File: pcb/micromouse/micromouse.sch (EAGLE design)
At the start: 57 parts, among them J1 Connector_M1, J2 Connector_M1, J4 Programmer

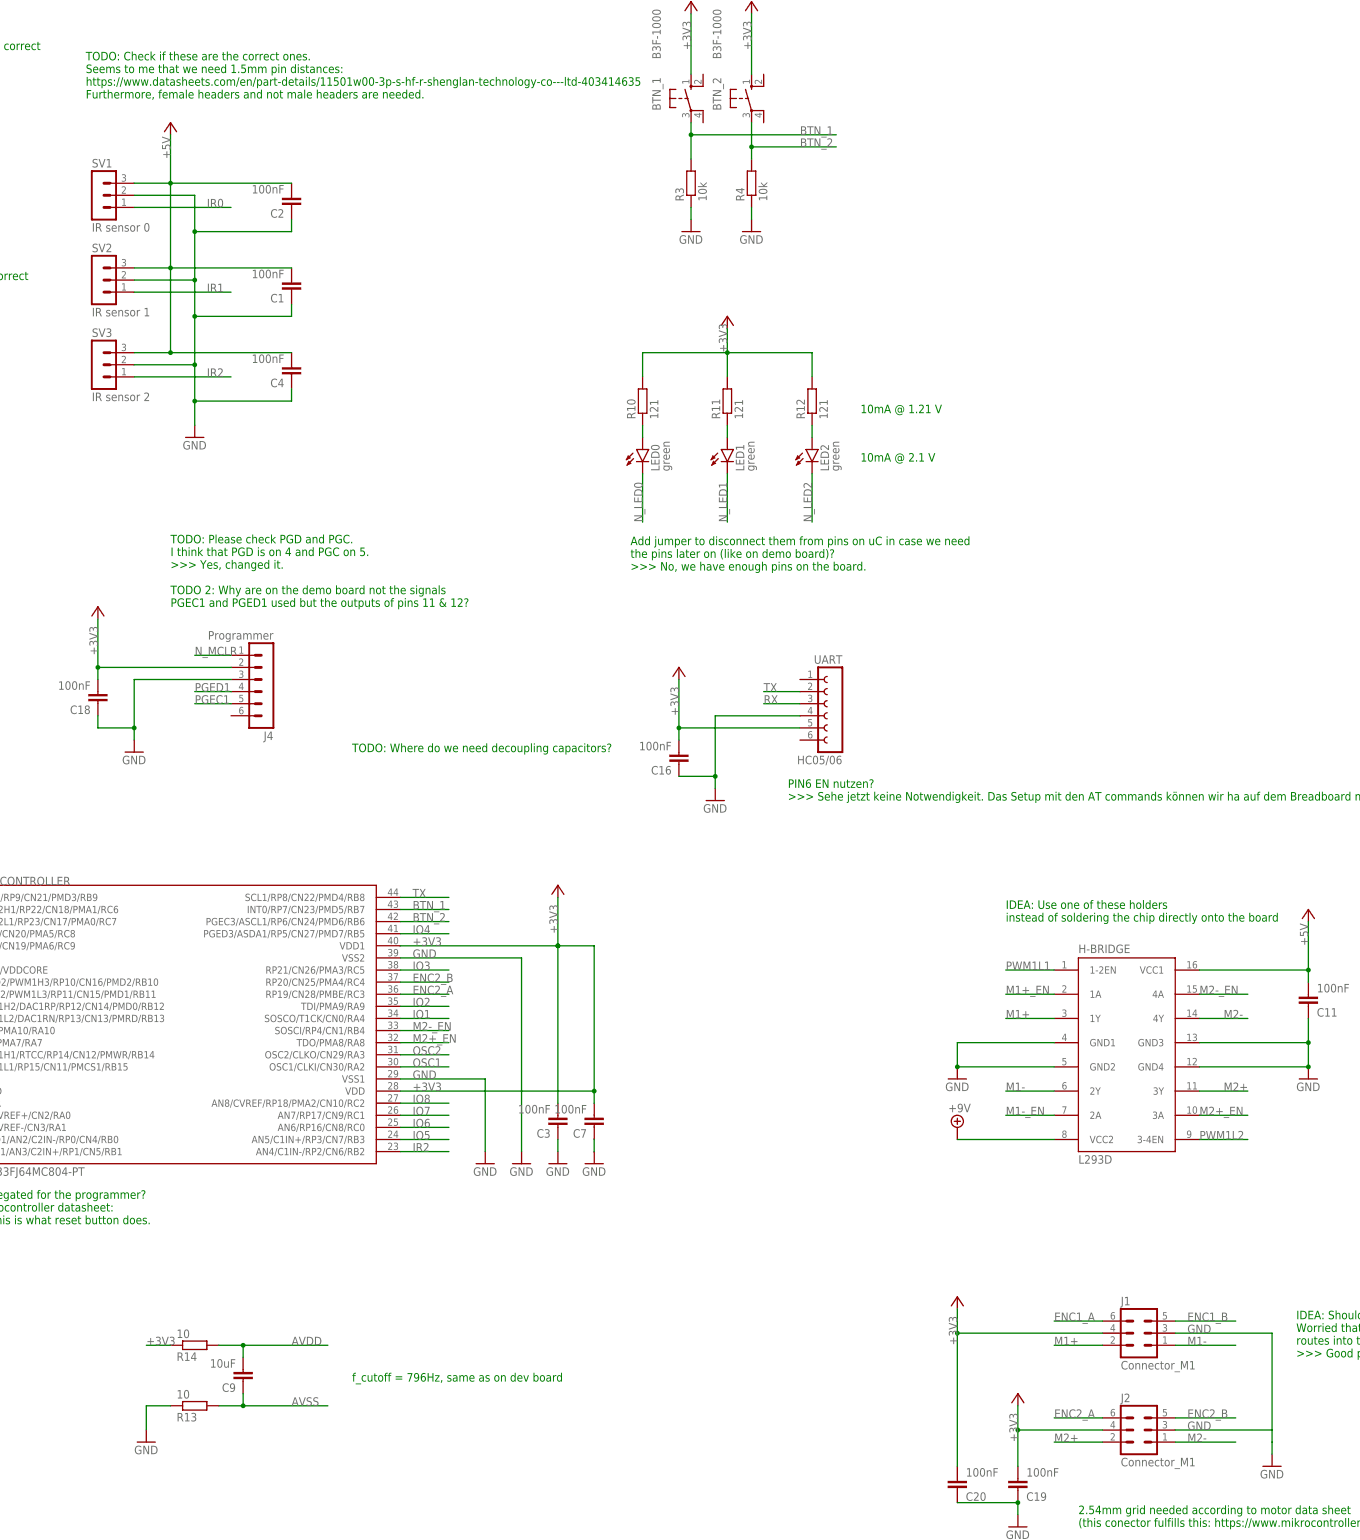
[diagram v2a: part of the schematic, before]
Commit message: Add missing junction (two wires were not correctly connected).
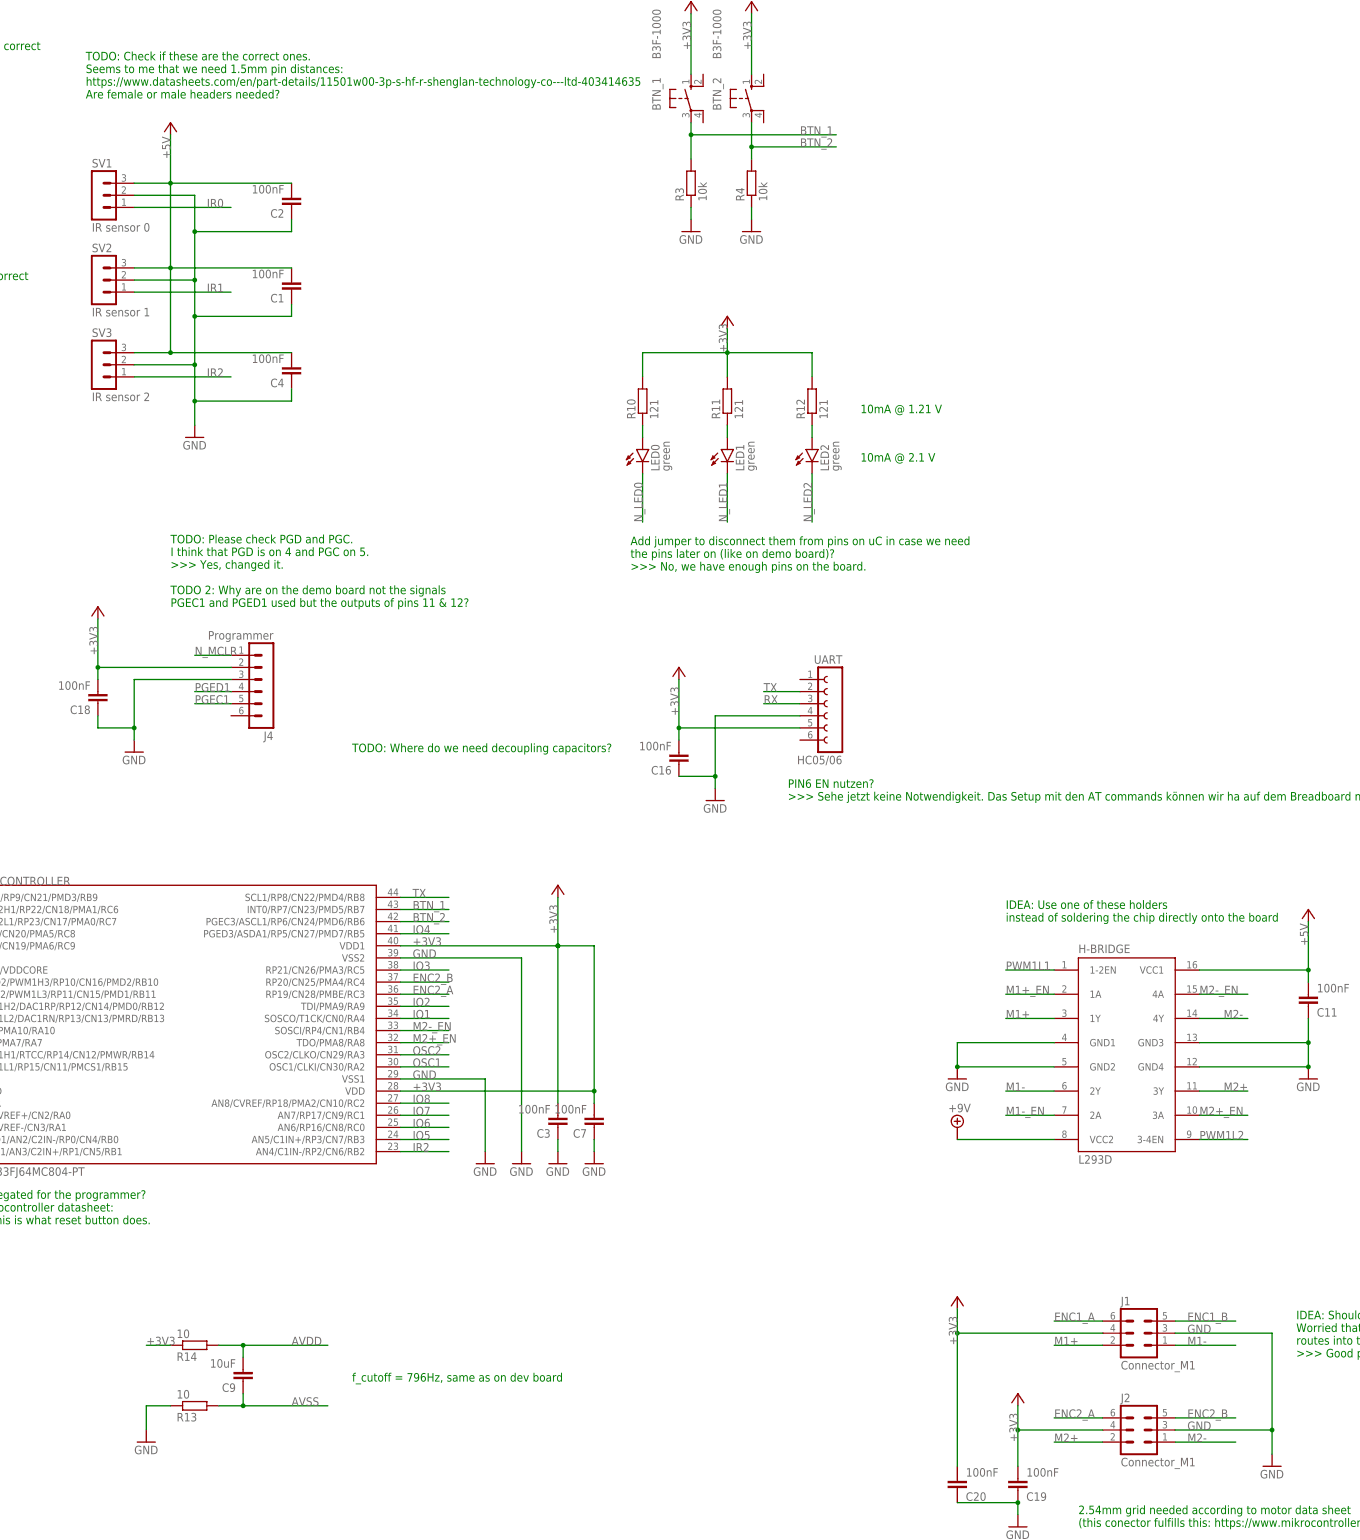
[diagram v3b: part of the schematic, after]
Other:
- note added: "TODO: Check if these are the correct ones. Seems to me that we need 1.5mm pin distances: https://www.datasheets.com/en/part-details/11501w00-3p-s-hf-r-shenglan-technology-co---ltd-403414635 Are female or male headers needed?"
- note removed: "TODO: Check if these are the correct ones. Seems to me that we need 1.5mm pin distances: https://www.datasheets.com/en/part-details/11501w00-3p-s-hf-r-shenglan-technology-co---ltd-403414635 Furthermore, female headers and not male headers are needed."
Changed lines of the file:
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@@
 Seems to me that we need 1.5mm pin distances:
 https://www.datasheets.com/en/part-details/11501w00-3p-s-hf-r-shenglan-technology-co---ltd-403414635
-Furthermore, female headers and not male headers are needed.</text>
+Are female or male headers needed?</text>
 <text x="-71.12" y="358.14" size="1.778" layer="91">Connects either 2-3 or 2-1,
 depending on switch position.</text>
@@
 </segment>
 <segment>
-<pinref part="J2" gate="1" pin="3"/>
-<wire x1="330.2" y1="48.26" x2="350.52" y2="48.26" width="0.1524" layer="91"/>
 <label x="332.74" y="48.26" size="1.778" layer="95"/>
 <pinref part="GND25" gate="1" pin="GND"/>
-<wire x1="350.52" y1="48.26" x2="350.52" y2="45.72" width="0.1524" layer="91"/>
-<wire x1="350.52" y1="45.72" x2="350.52" y2="43.18" width="0.1524" layer="91"/>
 <wire x1="330.2" y1="68.58" x2="350.52" y2="68.58" width="0.1524" layer="91"/>
 <pinref part="J1" gate="1" pin="3"/>
 <label x="332.74" y="68.58" size="1.778" layer="95"/>
 <wire x1="350.52" y1="68.58" x2="350.52" y2="48.26" width="0.1524" layer="91"/>
-</segment>
-<segment>
+<pinref part="J2" gate="1" pin="3"/>
+<wire x1="350.52" y1="48.26" x2="350.52" y2="43.18" width="0.1524" layer="91"/>
+<wire x1="330.2" y1="48.26" x2="350.52" y2="48.26" width="0.1524" layer="91"/>
+<junction x="350.52" y="48.26"/>
+</segment>
+<segment>

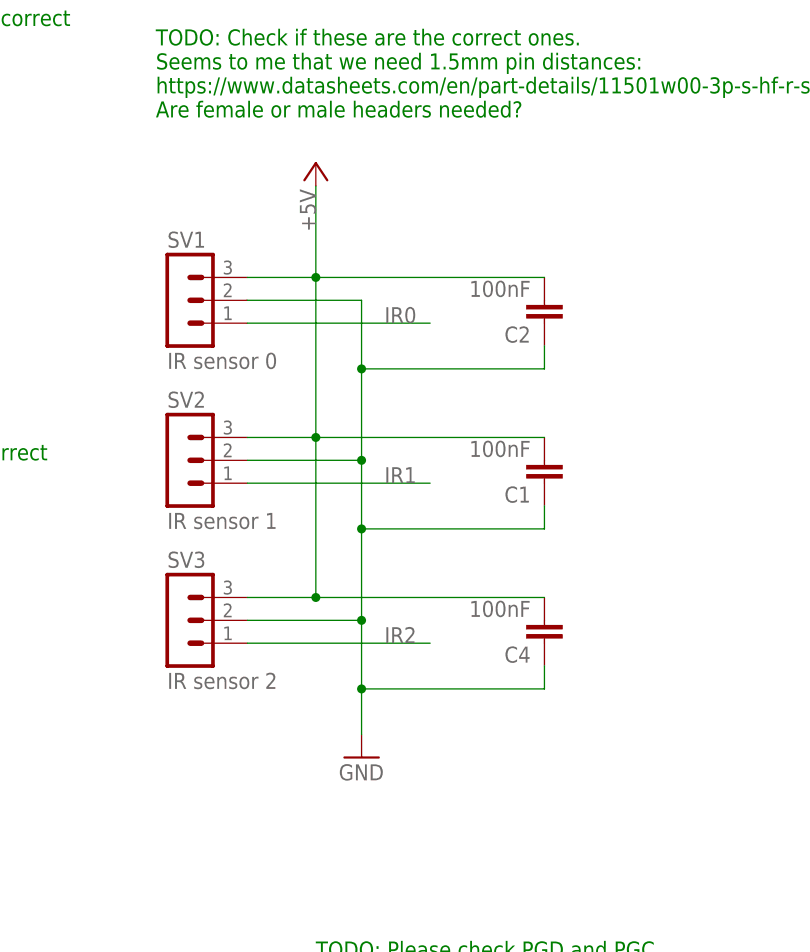
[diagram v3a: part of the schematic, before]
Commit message: Fix connection of IR sensors
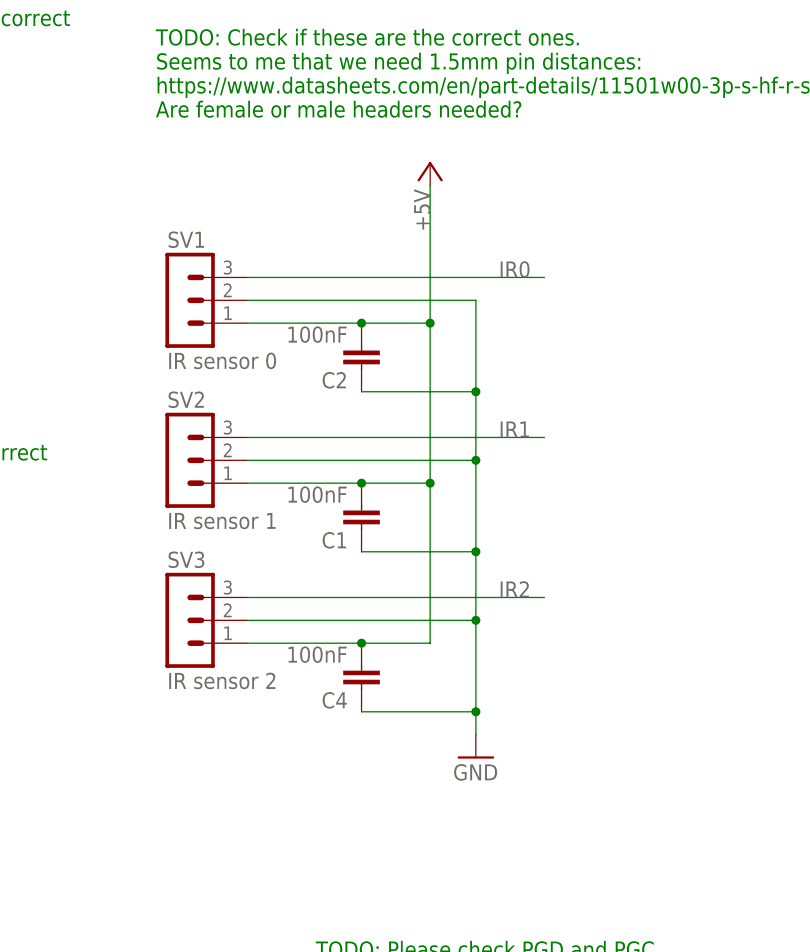
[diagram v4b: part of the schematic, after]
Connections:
- net +5V: now also SV1.1, SV2.1, SV3.1; no longer SV1.3, SV2.3, SV3.3
- net IR0: now also SV1.3; no longer SV1.1
- net IR1: now also SV2.3; no longer SV2.1
- net IR2: now also SV3.3; no longer SV3.1
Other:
- moved on the sheet: C1, C2, C4

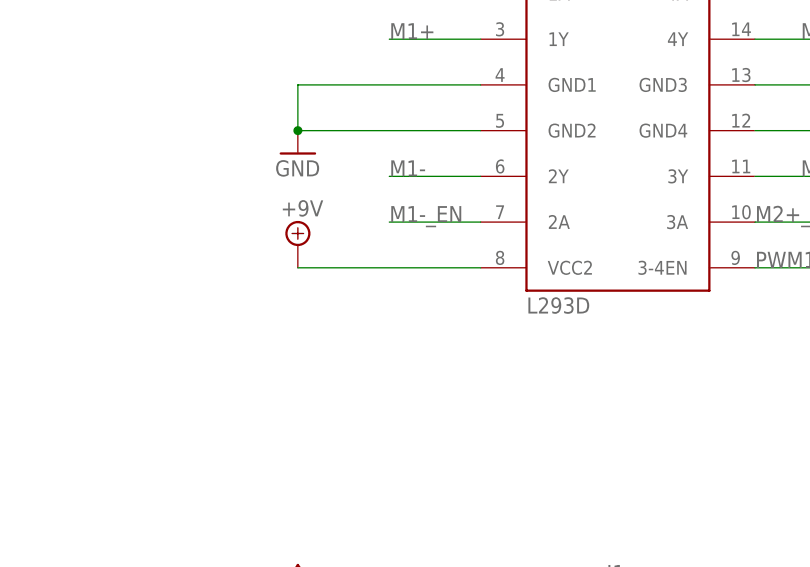
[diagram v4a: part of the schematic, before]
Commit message: Additional comment to have coupling capacitor at h bridge
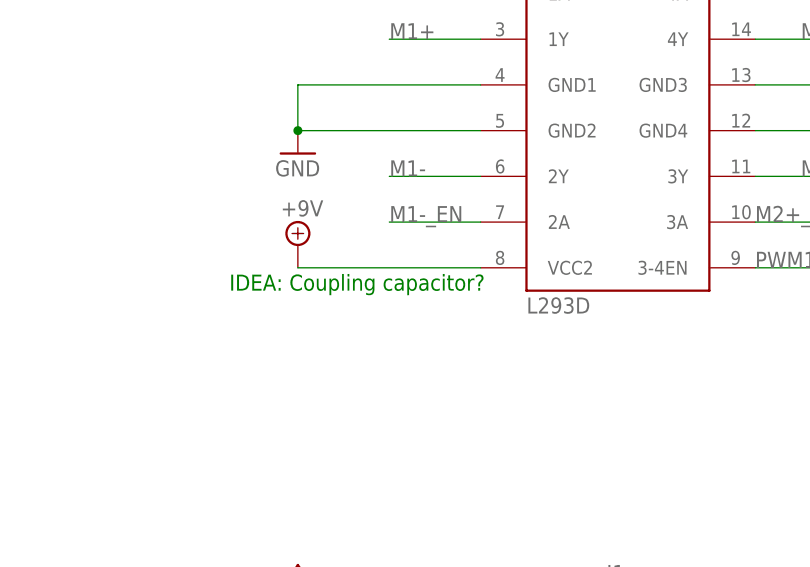
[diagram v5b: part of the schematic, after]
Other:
- note added: "IDEA: Coupling capacitor?"
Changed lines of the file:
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@@
 depending on switch position.</text>
 <text x="33.02" y="289.56" size="1.778" layer="91">TODO: Ask Lenz if external components are correct</text>
+<text x="276.86" y="106.68" size="1.778" layer="91">IDEA: Coupling capacitor?</text>
 </plain>
 <instances>

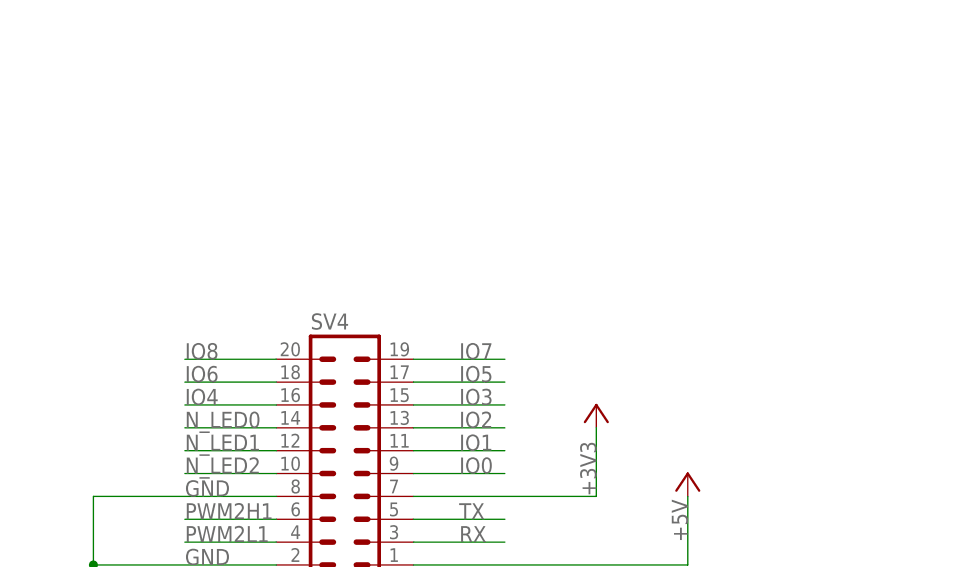
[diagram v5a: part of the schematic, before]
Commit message: Additional comment regarding helper header
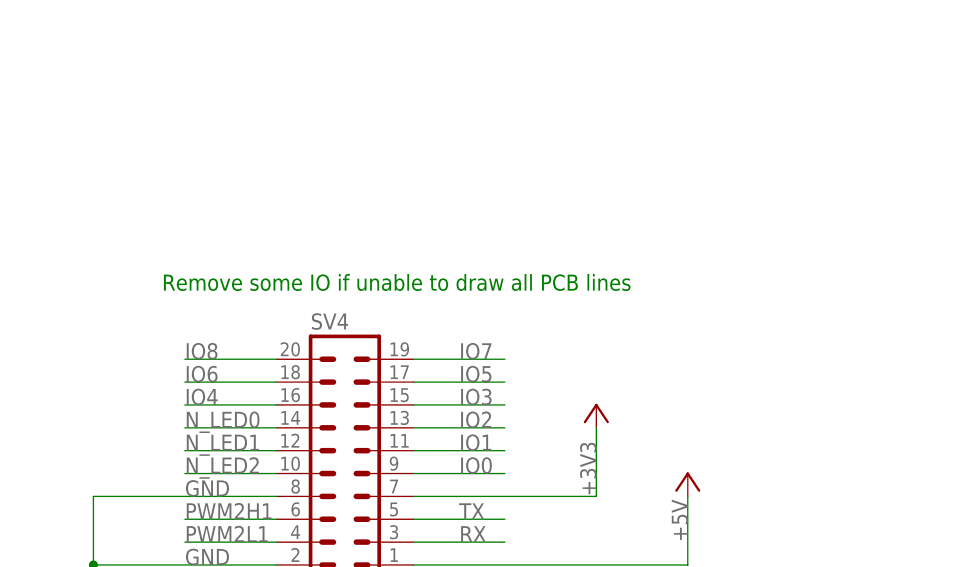
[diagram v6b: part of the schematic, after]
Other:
- note added: "Remove some IO if unable to draw all PCB lines"
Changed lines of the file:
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@@
 <text x="33.02" y="289.56" size="1.778" layer="91">TODO: Ask Lenz if external components are correct</text>
 <text x="276.86" y="106.68" size="1.778" layer="91">IDEA: Coupling capacitor?</text>
+<text x="-58.42" y="223.52" size="1.778" layer="91">Remove some IO if unable to draw all PCB lines</text>
 </plain>
 <instances>
